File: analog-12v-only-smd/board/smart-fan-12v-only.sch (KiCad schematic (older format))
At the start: 31 parts, among them J1 KTY81/120, J2 12V_PWR, J3 12V_In, J4 FAN_Out, J5 FAN_Out, Q1 2N7000, Q2 FQP27P06, U1 LM358, U2 L7809, U3 NE555P

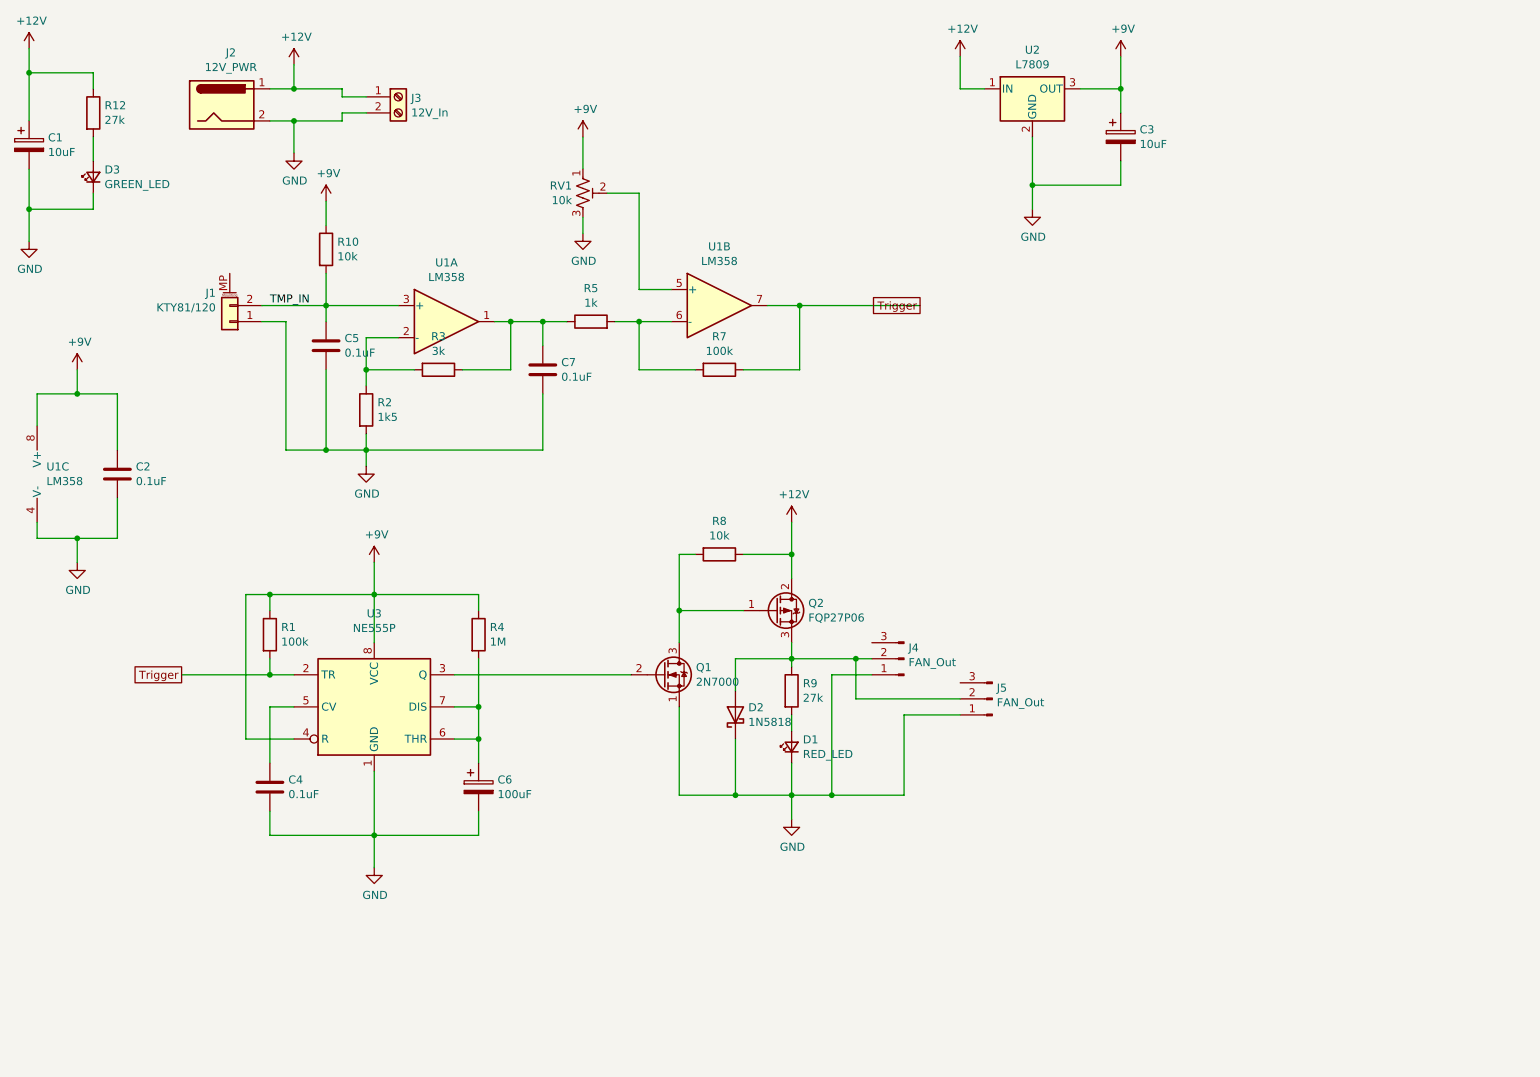
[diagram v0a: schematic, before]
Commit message: Fix board layout
Power transistor drain-source swapped
Flyback diode reversed
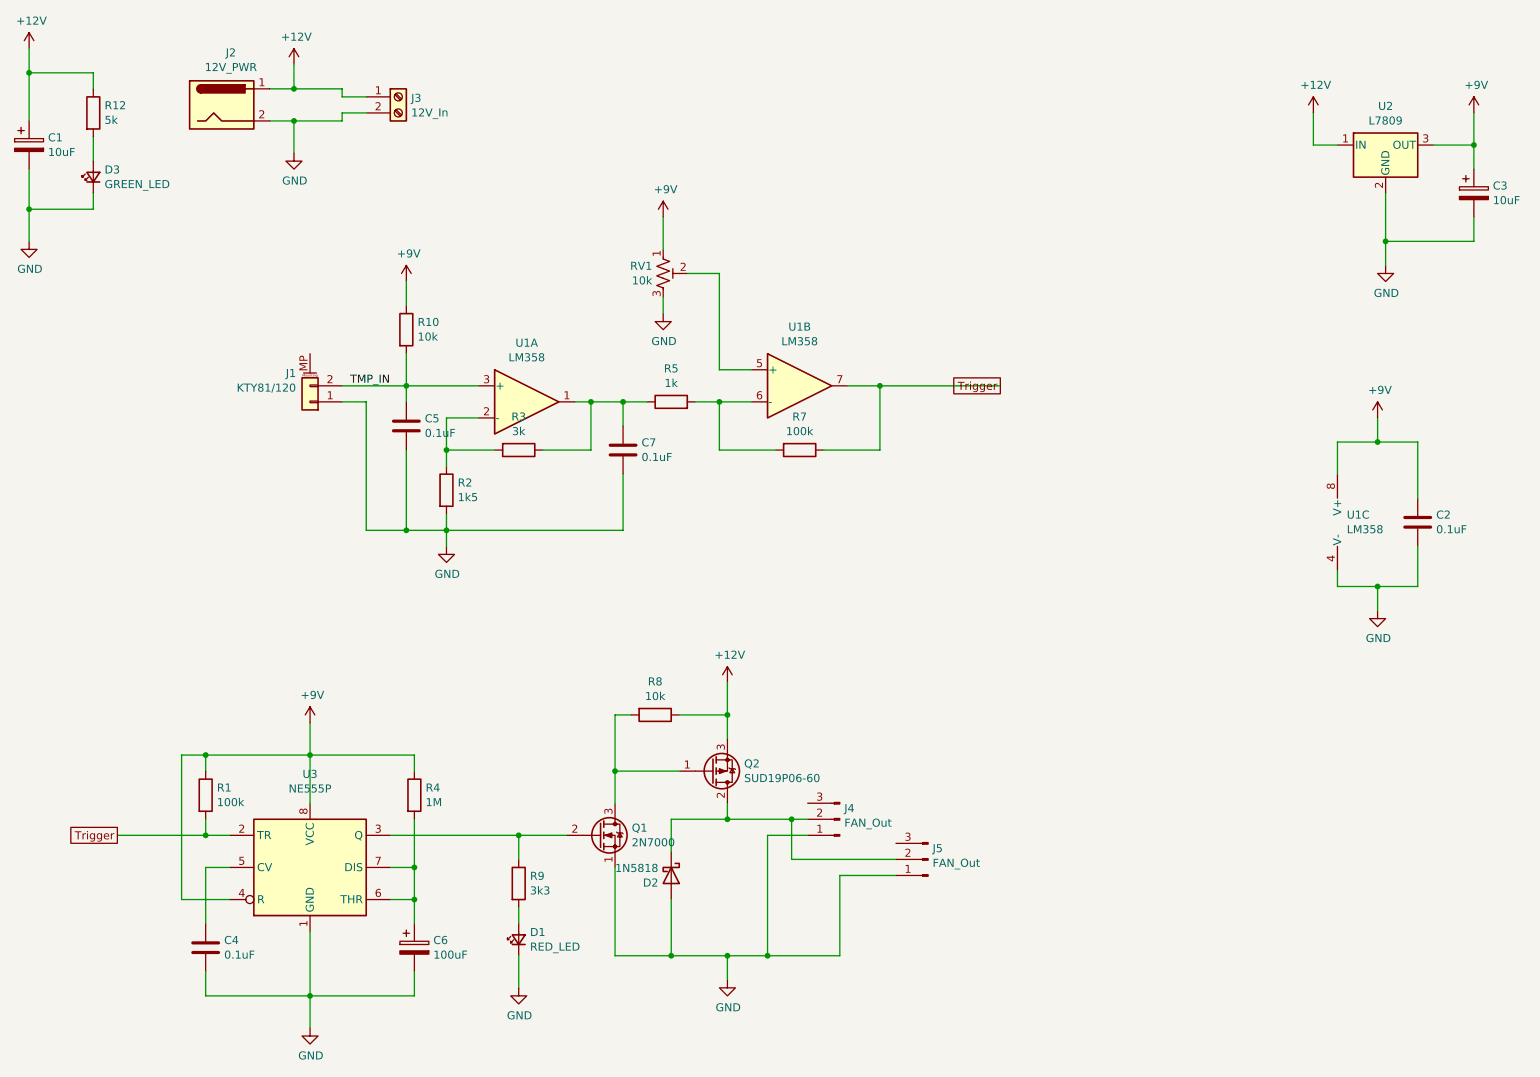
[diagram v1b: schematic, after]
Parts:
- removed Q2: FQP27P06, Package_TO_SOT_SMD:TO-263-2, symbol smart-fan-12v-only-rescue:FQP27P06-TransistorFET
- added Q2: SUD19P06-60, Package_TO_SOT_SMD:TO-252-2, symbol Transistor_FET:SUD19P06-60
- J3: footprint Connector_PinSocket_2.54mm:PinSocket_1x02_P2.54mm_Vertical -> TerminalBlock_Phoenix:TerminalBlock_Phoenix_MKDS-3-2-5.08_1x02_P5.08mm_Horizontal
- R12: value 27k -> 5k
- R9: value 27k -> 3k3
- RV1: footprint Resistor_SMD:R_0805_2012Metric -> Potentiometer_THT:Potentiometer_Bourns_3266Y_Vertical
- U2: footprint Package_TO_SOT_SMD:SOT-223 -> Package_TO_SOT_SMD:SOT-89-3
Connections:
- net +12V: now also Q2.3 (S)
- net GND: now also D2.2 (A); no longer D2.1 (K)
- net at Q1.2 (G), U3.3 (Q): now also R9.1
- net at Q1.3 (D), R8.2: now also Q2.1 (G)
- net at J4.2 (Pin_2), J5.2 (Pin_2): now also D2.1 (K), Q2.2 (D); no longer D2.2 (A), R9.1
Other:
- moved on the sheet: C2, C3, C4, C5, C6, C7, D1, D2, J1, J4, J5, Q1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

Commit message: WIP: Cleaning up board
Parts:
- D2: value 1N5818 -> 1N5819HW; footprint Diode_SMD:D_0805_2012Metric -> Diode_SMD:D_SOD-123
- Q2: value SUD19P06-60 -> DMP4051LK3-13
- R10: value 10k -> 100k
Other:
- moved on the sheet: D2
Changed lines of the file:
@@
 	4500 5850 4500 6400
 Wire Wire Line
-	4500 6400 4850 6400
+	4500 6400 5200 6400
 Wire Wire Line
 	3900 6600 3900 6400
@@
 L Device:D_Schottky D2
 U 1 1 5EEDDC4D
-P 4850 5900
-F 0 "D2" V 4896 5820 50  0000 R CNN
-F 1 "1N5818" V 4805 5820 50  0000 R CNN
-F 2 "Diode_SMD:D_0805_2012Metric" H 4850 5900 50  0001 C CNN
-F 3 "~" H 4850 5900 50  0001 C CNN
-	1    4850 5900
+P 5200 5950
+F 0 "D2" V 5246 5870 50  0000 R CNN
+F 1 "1N5819HW" V 5155 5870 50  0000 R CNN
+F 2 "Diode_SMD:D_SOD-123" H 5200 5950 50  0001 C CNN
+F 3 "~" H 5200 5950 50  0001 C CNN
+	1    5200 5950
 	0    1    1    0
 $EndComp
 Wire Wire Line
-	5200 5550 4850 5550
-Wire Wire Line
-	4850 5550 4850 5750
-Wire Wire Line
-	4850 6050 4850 6400
-Connection ~ 4850 6400
-Wire Wire Line
-	4850 6400 5200 6400
+	5200 6100 5200 6400
 Wire Wire Line
 	5900 5900 5900 6400
@@
 P 3200 2500
 F 0 "R10" H 3270 2546 50  0000 L CNN
-F 1 "10k" H 3270 2455 50  0000 L CNN
+F 1 "100k" H 3270 2455 50  0000 L CNN
 F 2 "Resistor_SMD:R_0805_2012Metric" V 3130 2500 50  0001 C CNN
 F 3 "~" H 3200 2500 50  0001 C CNN
@@
 P 5100 5250
 F 0 "Q2" H 5304 5204 50  0000 L CNN
-F 1 "SUD19P06-60" H 5304 5295 50  0000 L CNN
+F 1 "DMP4051LK3-13" H 5304 5295 50  0000 L CNN
 F 2 "Package_TO_SOT_SMD:TO-252-2" H 5295 5175 50  0001 L CIN
 F 3 "https://www.vishay.com/docs/69253/sud19p06.pdf" H 5100 5250 50  0001 C CNN
@@
 $EndComp
 $Comp
-L smart-fan-12v-only-rescue:GND-Power-smart-fan-rescue #PWR?
+L smart-fan-12v-only-rescue:GND-Power-smart-fan-rescue #PWR0118
 U 1 1 5F02ECF4
 P 3900 6600
-F 0 "#PWR?" H 3900 6350 50  0001 C CNN
+F 0 "#PWR0118" H 3900 6350 50  0001 C CNN
 F 1 "GND" H 3905 6427 50  0000 C CNN
 F 2 "" H 3900 6600 50  0001 C CNN
@@
 Wire Wire Line
 	3900 5650 4200 5650
+Wire Wire Line
+	5200 5550 5200 5800
 $EndSCHEMATC
